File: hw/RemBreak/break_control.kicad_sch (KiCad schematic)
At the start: 26 parts, among them J1 Conn_01x07, J12 Conn_01x04, J13 Conn_01x04, J14 Conn_01x03, J15 Conn_01x07, J16 Conn_01x03, J4 Conn_01x07, Q5 BC337, Q6 BC337, Q7 BC847, Q8 BC847

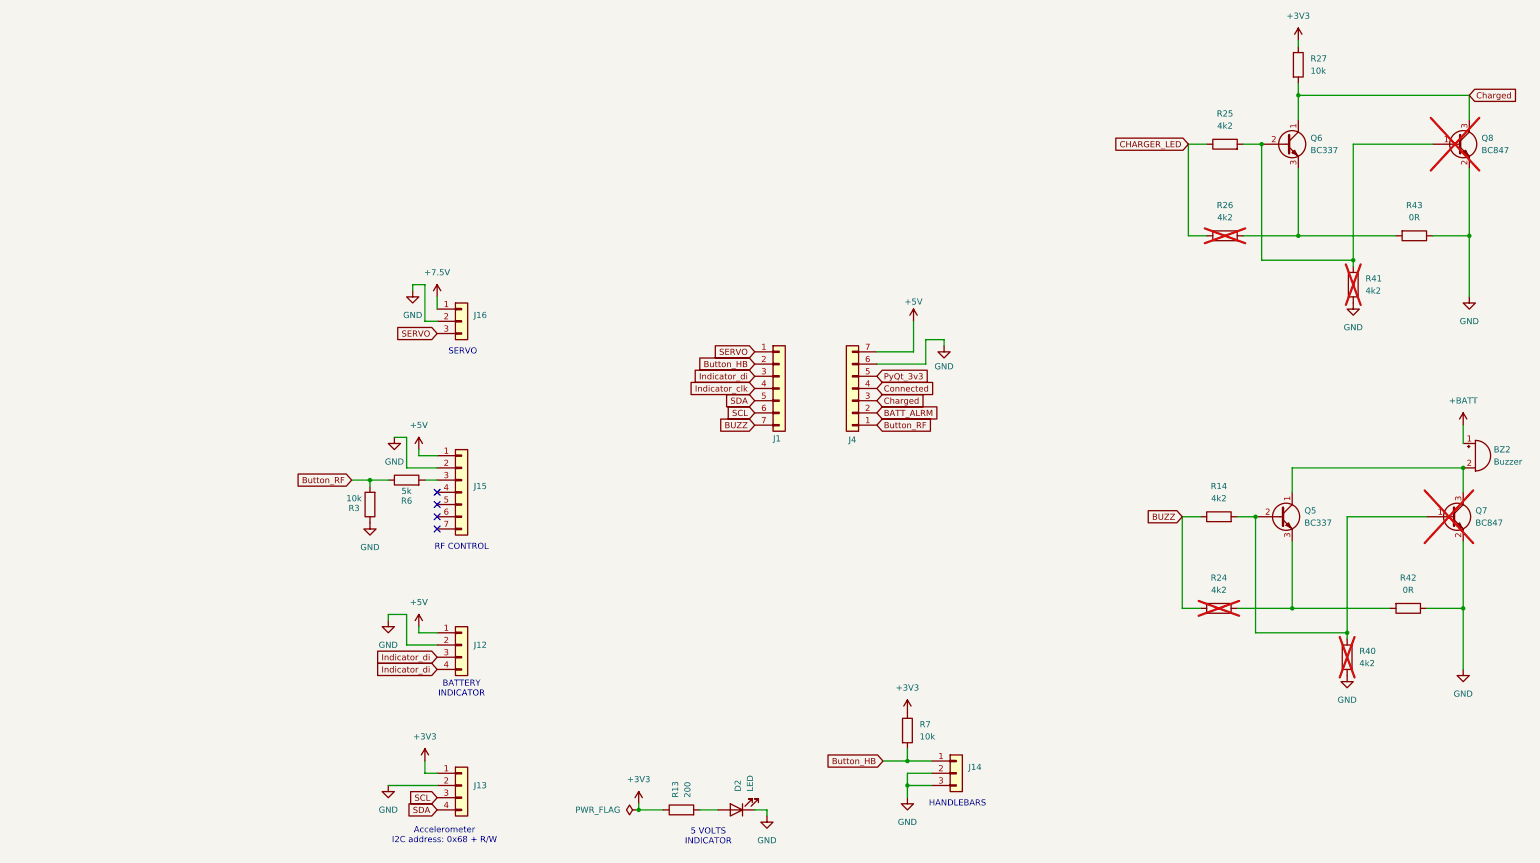
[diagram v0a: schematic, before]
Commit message: project update - started drawing the first revision of the board
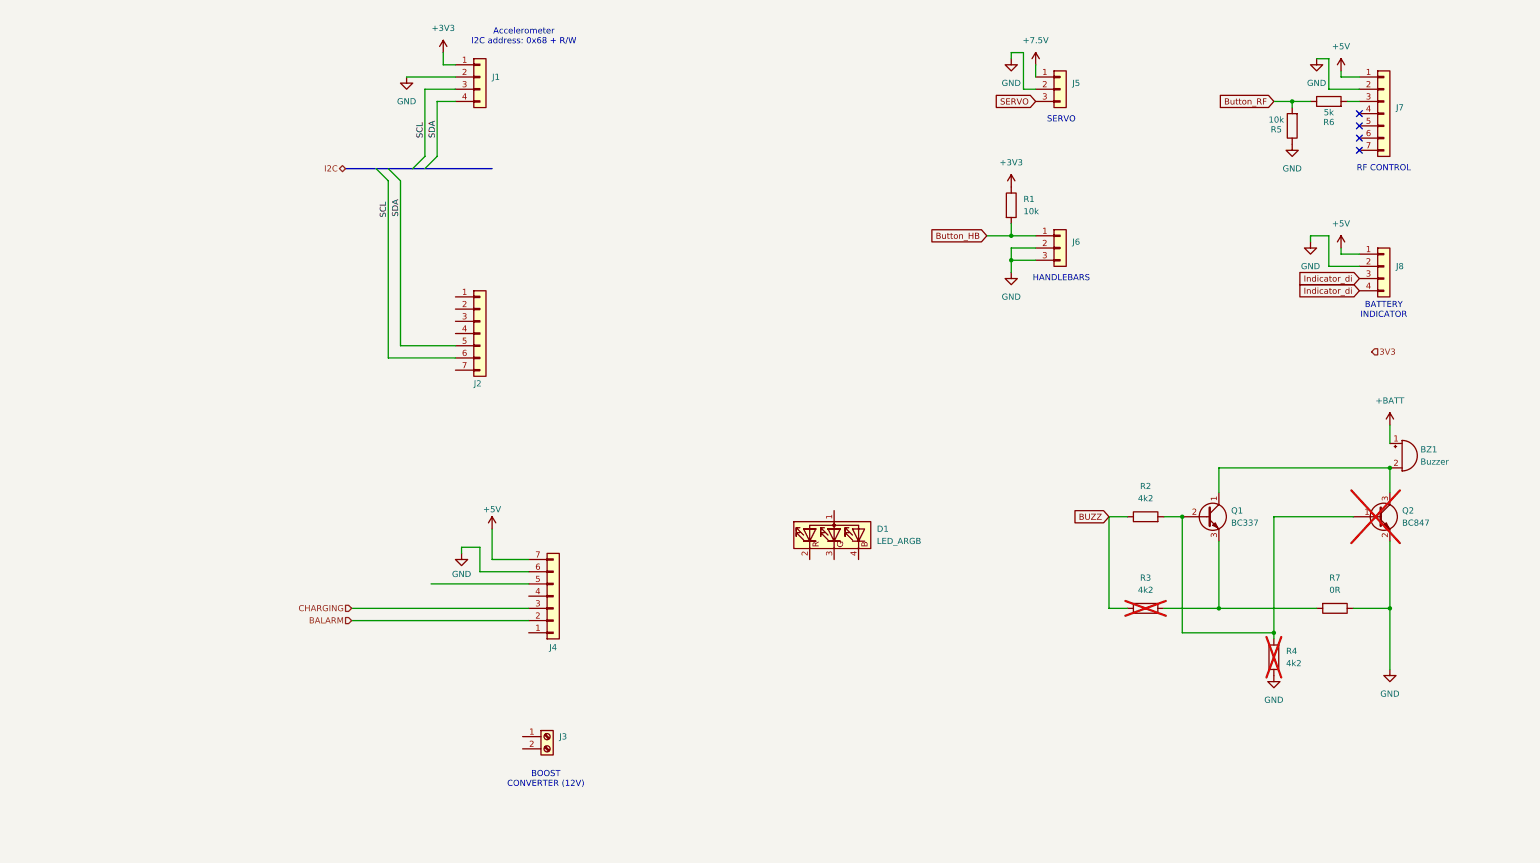
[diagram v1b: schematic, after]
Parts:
- removed D2: LED, symbol Device:LED
- removed Q6: BC337, Package_TO_SOT_THT:TO-92_Inline, symbol Transistor_BJT:BC337
- removed Q8: BC847, Package_TO_SOT_SMD:SOT-23, symbol Transistor_BJT:BC847
- removed R13: 200, symbol Device:R
- removed R25, R26, R41: 4k2, symbol Device:R
- removed R27: 10k, symbol Device:R
- removed R43: 0R, symbol Device:R
- added D1: LED_ARGB, LED_SMD:LED_WS2812B-Mini_PLCC4_3.5x3.5mm, symbol Device:LED_ARGB
- added J3: Screw_Terminal_01x02, TerminalBlock_Phoenix:TerminalBlock_Phoenix_MKDS-1,5-2_1x02_P5.00mm_Horizontal, symbol Connector:Screw_Terminal_01x02
- BZ1: renamed from BZ2; footprint (none) -> Buzzer_Beeper:Buzzer_12x9.5RM7.6
- J1: renamed from J13; footprint (none) -> Connector_PinSocket_2.54mm:PinSocket_1x04_P2.54mm_Vertical
- J2: renamed from J1; footprint (none) -> Connector_PinSocket_2.54mm:PinSocket_1x07_P2.54mm_Vertical
- J4: footprint (none) -> Connector_PinSocket_2.54mm:PinSocket_1x07_P2.54mm_Vertical
- J5: renamed from J16; footprint (none) -> Connector_PinHeader_2.54mm:PinHeader_1x03_P2.54mm_Vertical
- J6: renamed from J14; footprint (none) -> TerminalBlock_Phoenix:TerminalBlock_Phoenix_MKDS-1,5-2_1x02_P5.00mm_Horizontal
- J7: renamed from J15; footprint (none) -> Connector_PinSocket_2.54mm:PinSocket_1x07_P2.54mm_Vertical
- J8: renamed from J12; footprint (none) -> Connector_Molex:Molex_KK-254_AE-6410-04A_1x04_P2.54mm_Vertical
- R1: renamed from R7; footprint (none) -> Resistor_SMD:R_0805_2012Metric
- R2: renamed from R14; footprint (none) -> Resistor_SMD:R_0805_2012Metric
- R3: renamed from R24; footprint (none) -> Resistor_SMD:R_0805_2012Metric
- R4: renamed from R40; footprint (none) -> Resistor_SMD:R_0805_2012Metric
- R5: renamed from R3; footprint (none) -> Resistor_SMD:R_0805_2012Metric
- R6: footprint (none) -> Resistor_SMD:R_0805_2012Metric
- R7: renamed from R42; footprint (none) -> Resistor_SMD:R_0805_2012Metric
- renumbered Q5 to Q1, Q7 to Q2
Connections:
- net BUZZ: no longer J2.7 (Pin_7)
- net Button_HB: no longer J2.2 (Pin_2)
- net Button_RF: no longer J4.1 (Pin_1)
- net Indicator_di: no longer J2.3 (Pin_3)
- net SERVO: no longer J2.1 (Pin_1)
- net BATT_ALRM renamed BALARM
- net Charged renamed CHARGING
- net Connected: no longer names the net of J4.4 (Pin_4)
- net Indicator_clk: no longer names the net of J2.4 (Pin_4)
- net PyQt_3v3: no longer names the net of J4.5 (Pin_5)
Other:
- note added: "BOOST CONVERTER (12V)"
- note removed: "5 VOLTS INDICATOR"
- moved on the sheet: BZ1, J1, J2, J4, J5, J6, J7, J8, Q1, Q2, R1, R2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

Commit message: schematics drawing in progress
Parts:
- removed BZ1: Buzzer, Buzzer_Beeper:Buzzer_12x9.5RM7.6, symbol Device:Buzzer
- removed D1: LED_ARGB, LED_SMD:LED_WS2812B-Mini_PLCC4_3.5x3.5mm, symbol Device:LED_ARGB
- removed J3: Screw_Terminal_01x02, TerminalBlock_Phoenix:TerminalBlock_Phoenix_MKDS-1,5-2_1x02_P5.00mm_Horizontal, symbol Connector:Screw_Terminal_01x02
- removed J5: Conn_01x03, Connector_PinHeader_2.54mm:PinHeader_1x03_P2.54mm_Vertical, symbol Connector_Generic:Conn_01x03
- removed J6: Conn_01x03, TerminalBlock_Phoenix:TerminalBlock_Phoenix_MKDS-1,5-2_1x02_P5.00mm_Horizontal, symbol Connector_Generic:Conn_01x03
- removed J8: Conn_01x04, Connector_Molex:Molex_KK-254_AE-6410-04A_1x04_P2.54mm_Vertical, symbol Connector_Generic:Conn_01x04
- removed R1: 10k, Resistor_SMD:R_0805_2012Metric, symbol Device:R
- added C1, C2: 0.1uF, Capacitor_SMD:C_0805_2012Metric, symbol Device:C_Polarized
- added C3: 10uF, Capacitor_SMD:C_0805_2012Metric, symbol Device:C
- added J13: Conn_01x04, Connector_PinSocket_2.54mm:PinSocket_1x04_P2.54mm_Vertical, symbol Connector_Generic:Conn_01x04
- added J6, J7: Conn_01x01, TestPoint:TestPoint_Pad_2.5x2.5mm, symbol Connector_Generic:Conn_01x01
- added Q3: BC337, Package_TO_SOT_THT:TO-92_Inline, symbol Transistor_BJT:BC337
- added R10, R11: 10k, Resistor_SMD:R_0805_2012Metric, symbol Device:R
- added U1: SeeeduinoXIAO, chinese_modules:Seeeduino XIAO-MOUDLE14P-2.54-21X17.8MM, symbol chinese_modules:SeeeduinoXIAO
- added U2: L7805, Package_TO_SOT_SMD:TO-263-2, symbol Regulator_Linear:L7805
- added U3: L7805, Package_TO_SOT_THT:TO-220-3_Horizontal_TabDown, symbol Regulator_Linear:L7805
- added U4: XC6220B331MR, Package_TO_SOT_SMD:SOT-23-5, symbol Regulator_Linear:XC6220B331MR
- added U5: MAX40200AUK, Package_TO_SOT_SMD:SOT-23-5, symbol Analog_Switch:MAX40200AUK
- renumbered J7 to J4, J1 to J5, J2 to J8, J4 to J9, R2 to R4, R3 to R5, R5 to R7, R4 to R8, R7 to R9
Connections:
- net +3V3: now also J9.5 (Pin_5), R11.1, U5.5 (OUT)
- net +5V: now also J4.2 (Pin_2), C2.1, J13.3 (Pin_3), R10.2, U2.3 (OUT), U3.3 (OUT), U4.1 (VIN); no longer J4.1 (Pin_1), J9.7 (Pin_7)
- net BUZZ: now also J9.4 (Pin_4)
- net Button_RF: now also J8.2 (Pin_2)
- net GND: now also J4.1 (Pin_1), C1.2, C2.2, C3.2, J13.4 (Pin_4), Q3.3 (E), U2.2 (GND), U3.2 (GND), U4.2 (GND), U5.2 (GND); no longer J4.2 (Pin_2)
- net Indicator_di: now also J8.3 (Pin_3), J13.1 (Pin_1)
- net SERVO: now also J8.1 (Pin_1)
- net at Q1.1 (C), Q2.3 (C): now also J6.1 (Pin_1)
- net Indicator_dcki: now reaches J8.4 (Pin_4)
- net Indicator_dcki: now also J13.2 (Pin_2)
- net BUTTON: now reaches J8.7 (Pin_7)
- net BUTTON: now also R11.2
- new net: Q3.1 (C), R10.1, U4.3 (CE), U5.3 (EN)
- new net: C3.1, U4.5 (VOUT), U5.1 (VDD)
- new net BUZZ_pwr: J7.1 (Pin_1)
- new net EN: Q3.2 (B)
- new net PWR: C1.1, U2.1 (IN), U3.1 (IN)
- new net VBUS: J9.7 (Pin_7)
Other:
- note added: "BUZZER"
- note removed: "BOOST CONVERTER (12V)"
- note removed: "HANDLEBARS"
- note removed: "SERVO"
- moved on the sheet: J4, J5, J8, J9, Q1, Q2, R4, R5, R6, R7, R8, R9

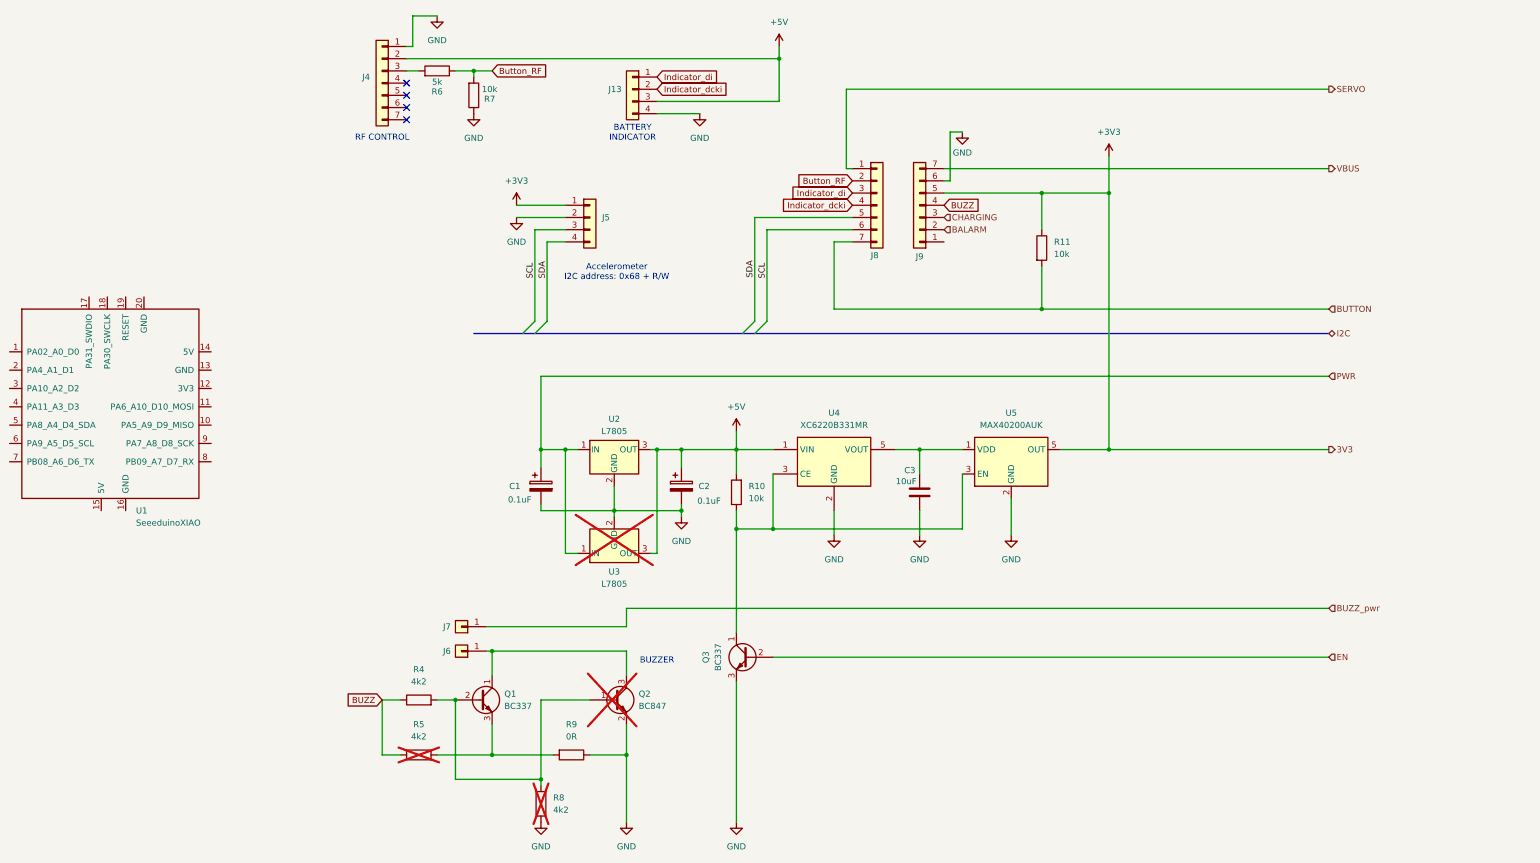
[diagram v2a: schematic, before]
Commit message: changes in power line sharing in progress
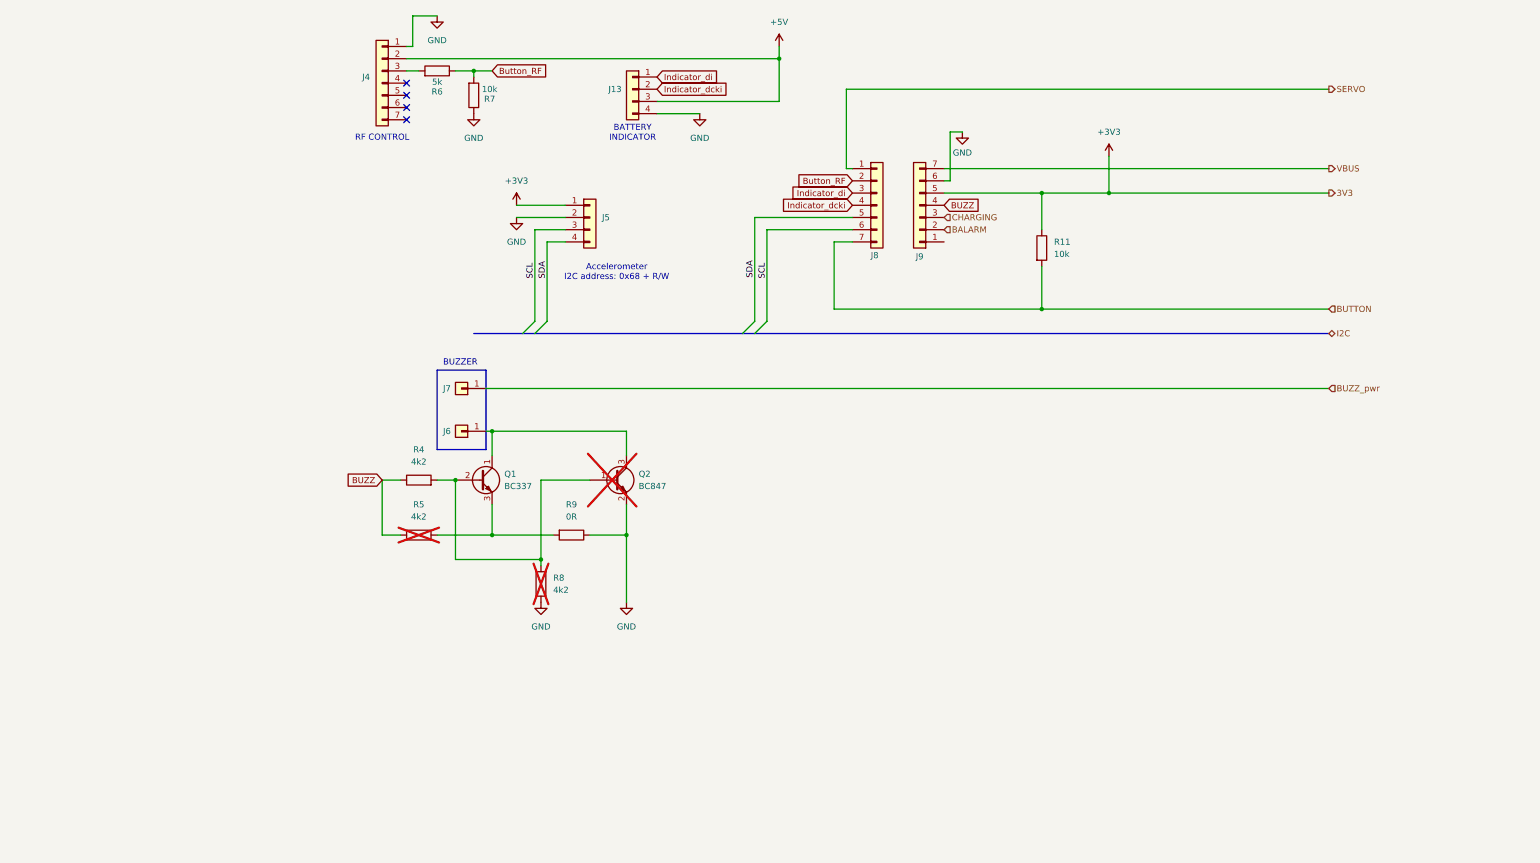
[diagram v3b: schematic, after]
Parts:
- removed C1, C2: 0.1uF, Capacitor_SMD:C_0805_2012Metric, symbol Device:C_Polarized
- removed C3: 10uF, Capacitor_SMD:C_0805_2012Metric, symbol Device:C
- removed Q3: BC337, Package_TO_SOT_THT:TO-92_Inline, symbol Transistor_BJT:BC337
- removed R10: 10k, Resistor_SMD:R_0805_2012Metric, symbol Device:R
- removed U1: SeeeduinoXIAO, chinese_modules:Seeeduino XIAO-MOUDLE14P-2.54-21X17.8MM, symbol chinese_modules:SeeeduinoXIAO
- removed U2: L7805, Package_TO_SOT_SMD:TO-263-2, symbol Regulator_Linear:L7805
- removed U3: L7805, Package_TO_SOT_THT:TO-220-3_Horizontal_TabDown, symbol Regulator_Linear:L7805
- removed U4: XC6220B331MR, Package_TO_SOT_SMD:SOT-23-5, symbol Regulator_Linear:XC6220B331MR
- removed U5: MAX40200AUK, Package_TO_SOT_SMD:SOT-23-5, symbol Analog_Switch:MAX40200AUK
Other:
- moved on the sheet: J6, J7, Q1, Q2, R4, R5, R8, R9

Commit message: schematics development in progress
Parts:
- removed J13, J5: Conn_01x04, Connector_PinSocket_2.54mm:PinSocket_1x04_P2.54mm_Vertical, symbol Connector_Generic:Conn_01x04
- removed J6, J7: Conn_01x01, TestPoint:TestPoint_Pad_2.5x2.5mm, symbol Connector_Generic:Conn_01x01
- added J1: Conn_01x03, Connector_PinHeader_2.54mm:PinHeader_1x03_P2.54mm_Vertical_SMD_Pin1Left, symbol Connector_Generic:Conn_01x03
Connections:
- net GND: now also J1.2 (Pin_2)
- net BUZZER: now reaches Q1.1 (C), Q2.3 (C)
- net +3V3 renamed 3V3
- net +5V renamed 5V
- net Indicator_dcki renamed Display_DI
- net Indicator_di renamed Display_DCKI
- net SERVO: no longer names the net of J8.1 (Pin_1)
- net SERVO: now also J1.3 (Pin_3)
- new net 7V4: J1.1 (Pin_1)
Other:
- note added: "SERVO"
- note removed: "Accelerometer I2C address: 0x68 + R/W"
- note removed: "BATTERY INDICATOR"
- note removed: "BUZZER"
- moved on the sheet: J4, J8, J9, Q1, Q2, R11, R4, R5, R6, R7, R8, R9

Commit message: updated pcb and schematics - still in progress
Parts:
- J4, J8, J9: footprint Connector_PinSocket_2.54mm:PinSocket_1x07_P2.54mm_Vertical -> Connector_PinSocket_2.54mm:PinSocket_1x07_P2.54mm_Vertical_SMD_Pin1Left
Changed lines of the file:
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@@
 			)
 		)
-		(property "Footprint" "Connector_PinSocket_2.54mm:PinSocket_1x07_P2.54mm_Vertical"
+		(property "Footprint" "Connector_PinSocket_2.54mm:PinSocket_1x07_P2.54mm_Vertical_SMD_Pin1Left"
 			(at 143.51 93.98 0)
 			(effects
@@
 			)
 		)
-		(property "Footprint" "Connector_PinSocket_2.54mm:PinSocket_1x07_P2.54mm_Vertical"
+		(property "Footprint" "Connector_PinSocket_2.54mm:PinSocket_1x07_P2.54mm_Vertical_SMD_Pin1Left"
 			(at 59.69 68.58 0)
 			(effects
@@
 			)
 		)
-		(property "Footprint" "Connector_PinSocket_2.54mm:PinSocket_1x07_P2.54mm_Vertical"
+		(property "Footprint" "Connector_PinSocket_2.54mm:PinSocket_1x07_P2.54mm_Vertical_SMD_Pin1Left"
 			(at 134.62 93.98 0)
 			(effects

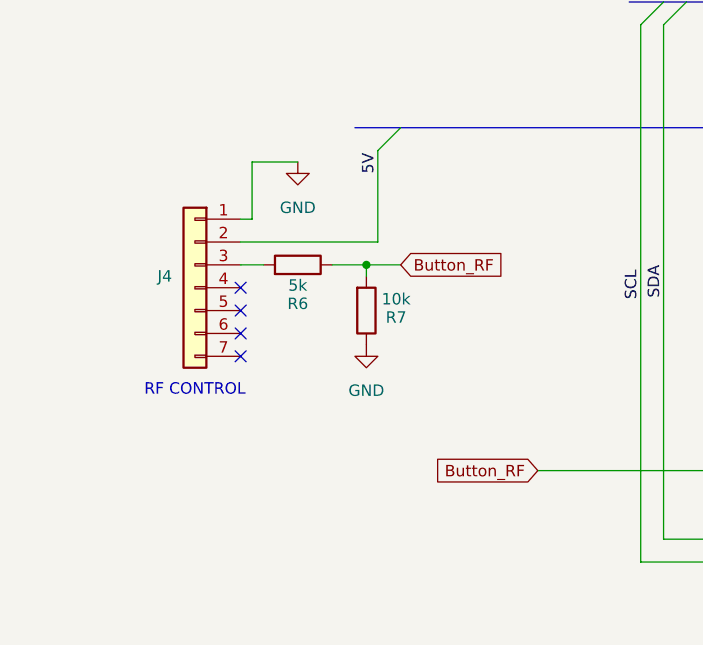
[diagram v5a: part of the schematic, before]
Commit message: changed size of the board and development of schematic
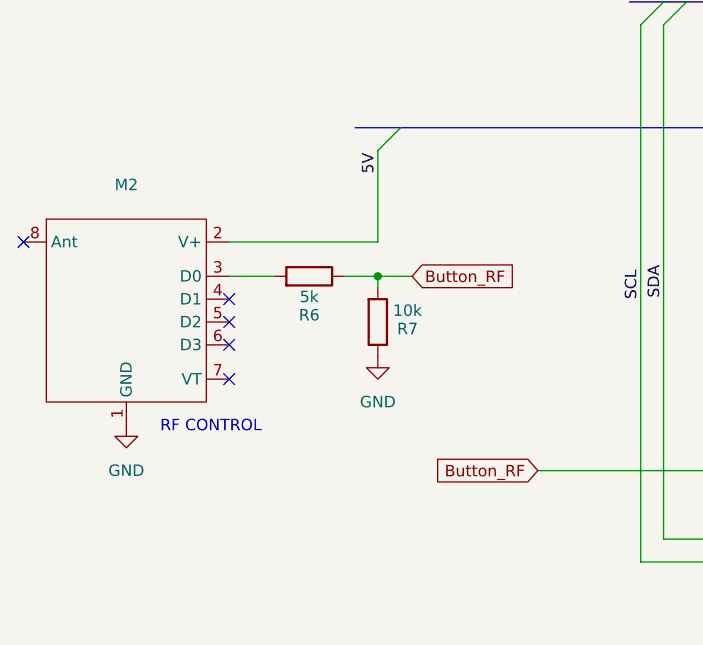
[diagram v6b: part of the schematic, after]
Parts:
- removed J4: Conn_01x07, Connector_PinSocket_2.54mm:PinSocket_1x07_P2.54mm_Vertical_SMD_Pin1Left, symbol Connector_Generic:Conn_01x07
- added M2: ~, chinese_modules:RF_controller, symbol chinese_modules:RF_controller
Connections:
- net 5V: now also M2.2 (V+)
- net GND: now also M2.1 (GND)
- net at R6.2: now also M2.3 (D0)
- no-connect marks 4 -> 5
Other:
- moved on the sheet: R6, R7

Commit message: finished schematics routing and erc passed
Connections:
- net 3V3 renamed +3V3
- net 5V renamed +5V
- net 7V4 renamed +7.5V
- net Button_RF: no longer names the net of J8.2 (Pin_2), R6.1, R7.2
- net Display_DCKI renamed DISPLAY.DCKI
- net Display_DI renamed DISPLAY.DI
- net SCL renamed I2C.SCL
- net SDA renamed I2C.SDA
- no-connect marks 5 -> 6
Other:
- note added: "RF (BUTTON) CONTROL"
- note added: "TODO: Add zener diode (3V3)"
- note removed: "RF CONTROL"
- moved on the sheet: M2, R6, R7
